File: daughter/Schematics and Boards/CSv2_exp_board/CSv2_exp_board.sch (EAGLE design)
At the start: 144 parts, among them J1 HIROSE-DF40_44-PIN_CONNECTORS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, J2 J-SERIAL-PORT, J3 CORTEX_DEBUG_SMD, J4 SJ-43514-SMT, J5 HIROSE-DF40_44-PIN_CONNECTORS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, J6 ATTINY_AVR_DEBUG, J7 J-USB-HIROSE-MICRO-USB, SW1 SPST_TACT-KMR2, SW2 SPST_TACT-KMR2, T1 TPTP10SQ, T10 TPTP10SQ, T11 TPTP10SQ, T2 TPTP10SQ, T3 TPTP10SQ, T4 TPTP10SQ, T5 TPTP10SQ, T6 TPTP10SQ, T7 TPTP10SQ, T8 TPTP10SQ, T9 TPTP10SQ, U1 LOADSWITCH-MIC94164, U10 LOADSWITCH-MIC94164, U11 BMI160, U12 TLV320DAC26IRHB, U13 ADG839YKSZ-500RL7KS_6_ADI-L, U14 LOADSWITCH-MIC94164, U15 LP2980AIM5-2.5/NOPBMF05A_TEX-L, U16 NCP553SQ18T1GSC-82AB_ONS-L, U17 ATTINY817-MFRQFN24_RX4MC-L_AT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, U18 MPL3115A2, U19 ATSAMD21G18_QFN, U2 ADA4841-1YRJZ-R7RJ_6-L, U3 Value, U4 RFM69HCW, U5 Value, U6 Value, U7 LOADSWITCH-MIC94164, U8 LOADSWITCH-MIC94164, U9 LOADSWITCH-MIC94164, X1 32.768kHz, X2 32.768, X3 uFL, X4 uFL, X5 uFL, X6 uFL

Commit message: DTR-filled in device attributes
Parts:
- X2: value 32.768 -> 32.768kHz; DESC (none) -> CRYSTAL 32.7680KHZ 6PF SMD; HEIGHT (none) -> 0.9mm; LOAD_CAPACITY 6p -> 6pF; SIZE (none) -> 0.126" L x 0.059" W (3.20mm x 1.50mm); TOL (none) -> ±20ppm; TYPE (none) -> Crystal
- X3, X5, X6: DESC (none) -> CONN U.FL RCPT STR 50 OHM SMD; HEIGHT d -> 1.25mm; MANUFACTURER (none) -> Hirose; SIZE (none) -> 3.1 x 3mm; TYPE (none) -> Connector
- X4: DESC (none) -> CONN U.FL RCPT STR 50 OHM SMD; HEIGHT (none) -> 1.25mm; MEANUFACTURER (none) -> Hirose; SIZE (none) -> 3.1 x 3mm; TYPE (none) -> Connector
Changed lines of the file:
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@@
 <attribute name="Z-HEIGHT" value="0.55mm"/>
 </part>
-<part name="X2" library="CommonSense-DTR-v1" deviceset="ADAFRUIT2_XTAL" device="-3.2X1.5" value="32.768">
-<attribute name="DESC" value=""/>
-<attribute name="LOAD_CAPACITY" value="6p"/>
+<part name="X2" library="CommonSense-DTR-v1" deviceset="ADAFRUIT2_XTAL" device="-3.2X1.5" value="32.768kHz">
+<attribute name="DESC" value="CRYSTAL 32.7680KHZ 6PF SMD"/>
+<attribute name="HEIGHT" value="0.9mm"/>
+<attribute name="LOAD_CAPACITY" value="6pF"/>
 <attribute name="MANUFACTURER" value="NDK"/>
 <attribute name="MPN" value="NX3215SA-32.768K-STD-MUA-14"/>
 <attribute name="PARTNO" value="NX3215SA-32.768K-STD-MUA-14"/>
-<attribute name="SIZE" value=""/>
-<attribute name="TOL" value=""/>
-<attribute name="TYPE" value=""/>
-<attribute name="VOLT" value=""/>
+<attribute name="SIZE" value="0.126&quot; L x 0.059&quot; W (3.20mm x 1.50mm)"/>
+<attribute name="TOL" value="±20ppm"/>
+<attribute name="TYPE" value="Crystal"/>
 </part>
 <part name="U$14" library="Supplies" deviceset="GND" device=""/>
@@
 <part name="U$17" library="Supplies" deviceset="GND" device=""/>
 <part name="X4" library="Connectors" deviceset="J-U.FL" device="" value="uFL">
-<attribute name="DESC" value=""/>
+<attribute name="DESC" value="CONN U.FL RCPT STR 50 OHM SMD"/>
+<attribute name="HEIGHT" value="1.25mm"/>
+<attribute name="MEANUFACTURER" value="Hirose"/>
 <attribute name="MPN" value="U.FL-R-SMT-1(01)"/>
 <attribute name="PARTNO" value="U.FL-R-SMT-1(01)"/>
-<attribute name="SIZE" value=""/>
-<attribute name="TOL" value=""/>
-<attribute name="TYPE" value=""/>
-<attribute name="VOLT" value=""/>
+<attribute name="SIZE" value="3.1 x 3mm"/>
+<attribute name="TYPE" value="Connector"/>
 </part>
 <part name="U$23" library="Supplies" deviceset="GND" device=""/>
@@
 </part>
 <part name="X3" library="Connectors" deviceset="J-U.FL" device="" value="uFL">
-<attribute name="HEIGHT" value="d"/>
+<attribute name="DESC" value="CONN U.FL RCPT STR 50 OHM SMD"/>
+<attribute name="HEIGHT" value="1.25mm"/>
+<attribute name="MANUFACTURER" value="Hirose"/>
 <attribute name="MPN" value="U.FL-R-SMT-1(01)"/>
 <attribute name="PARTNO" value="U.FL-R-SMT-1(01)"/>
+<attribute name="SIZE" value="3.1 x 3mm"/>
+<attribute name="TYPE" value="Connector"/>
 </part>
 <part name="X5" library="Connectors" deviceset="J-U.FL" device="" value="uFL">
-<attribute name="HEIGHT" value="d"/>
+<attribute name="DESC" value="CONN U.FL RCPT STR 50 OHM SMD"/>
+<attribute name="HEIGHT" value="1.25mm"/>
+<attribute name="MANUFACTURER" value="Hirose"/>
 <attribute name="MPN" value="U.FL-R-SMT-1(01)"/>
 <attribute name="PARTNO" value="U.FL-R-SMT-1(01)"/>
+<attribute name="SIZE" value="3.1 x 3mm"/>
+<attribute name="TYPE" value="Connector"/>
 </part>
 <part name="X6" library="Connectors" deviceset="J-U.FL" device="" value="uFL">
-<attribute name="HEIGHT" value="d"/>
+<attribute name="DESC" value="CONN U.FL RCPT STR 50 OHM SMD"/>
+<attribute name="HEIGHT" value="1.25mm"/>
+<attribute name="MANUFACTURER" value="Hirose"/>
 <attribute name="MPN" value="U.FL-R-SMT-1(01)"/>
 <attribute name="PARTNO" value="U.FL-R-SMT-1(01)"/>
+<attribute name="SIZE" value="3.1 x 3mm"/>
+<attribute name="TYPE" value="Connector"/>
 </part>
 <part name="R7" library="Resistors" deviceset="R-" device="0402" value="50R">
@@
 <attribute name="TYPE" x="284.48" y="231.14" size="1.778" layer="96" display="off"/>
 <attribute name="SIZE" x="284.48" y="231.14" size="1.778" layer="96" display="off"/>
-<attribute name="VOLT" x="284.48" y="231.14" size="1.778" layer="96" display="off"/>
+<attribute name="HEIGHT" x="284.48" y="231.14" size="1.778" layer="96" display="off"/>
 </instance>
 <instance part="U$14" gate="1" x="101.6" y="233.68" smashed="yes">
@@
 <attribute name="MPN" x="78.62295625" y="212.957171875" size="1.778" layer="96" rot="R90" display="off"/>
 <attribute name="PARTNO" x="78.62295625" y="212.957171875" size="1.778" layer="96" display="off"/>
-<attribute name="TOL" x="78.62295625" y="212.957171875" size="1.778" layer="96" rot="R90" display="off"/>
 <attribute name="DESC" x="78.62295625" y="212.957171875" size="1.778" layer="96" rot="R90" display="off"/>
 <attribute name="TYPE" x="78.62295625" y="212.957171875" size="1.778" layer="96" rot="R90" display="off"/>
 <attribute name="SIZE" x="78.62295625" y="212.957171875" size="1.778" layer="96" rot="R90" display="off"/>
-<attribute name="VOLT" x="78.62295625" y="212.957171875" size="1.778" layer="96" rot="R90" display="off"/>
+<attribute name="HEIGHT" x="78.62295625" y="212.957171875" size="1.778" layer="96" rot="R90" display="off"/>
+<attribute name="MEANUFACTURER" x="78.62295625" y="212.957171875" size="1.778" layer="96" rot="R90" display="off"/>
 </instance>
 <instance part="U$23" gate="1" x="68.58" y="215.9" smashed="yes">
@@
 <attribute name="MPN" x="266.58295625" y="248.517171875" size="1.778" layer="96" rot="R90" display="off"/>
 <attribute name="PARTNO" x="266.58295625" y="248.517171875" size="1.778" layer="96" display="off"/>
+<attribute name="SIZE" x="266.58295625" y="248.517171875" size="1.778" layer="96" rot="R90" display="off"/>
+<attribute name="DESC" x="266.58295625" y="248.517171875" size="1.778" layer="96" rot="R90" display="off"/>
+<attribute name="TYPE" x="266.58295625" y="248.517171875" size="1.778" layer="96" rot="R90" display="off"/>
+<attribute name="MANUFACTURER" x="266.58295625" y="248.517171875" size="1.778" layer="96" rot="R90" display="off"/>
 <attribute name="HEIGHT" x="266.58295625" y="248.517171875" size="1.778" layer="96" rot="R90" display="off"/>
 </instance>
@@
 <attribute name="MPN" x="297.06295625" y="248.517171875" size="1.778" layer="96" rot="R90" display="off"/>
 <attribute name="PARTNO" x="297.06295625" y="248.517171875" size="1.778" layer="96" display="off"/>
+<attribute name="SIZE" x="297.06295625" y="248.517171875" size="1.778" layer="96" rot="R90" display="off"/>
+<attribute name="DESC" x="297.06295625" y="248.517171875" size="1.778" layer="96" rot="R90" display="off"/>
+<attribute name="TYPE" x="297.06295625" y="248.517171875" size="1.778" layer="96" rot="R90" display="off"/>
+<attribute name="MANUFACTURER" x="297.06295625" y="248.517171875" size="1.778" layer="96" rot="R90" display="off"/>
 <attribute name="HEIGHT" x="297.06295625" y="248.517171875" size="1.778" layer="96" rot="R90" display="off"/>
 </instance>
@@
 <attribute name="MPN" x="330.08295625" y="248.517171875" size="1.778" layer="96" rot="R90" display="off"/>
 <attribute name="PARTNO" x="330.08295625" y="248.517171875" size="1.778" layer="96" display="off"/>
+<attribute name="SIZE" x="330.08295625" y="248.517171875" size="1.778" layer="96" rot="R90" display="off"/>
+<attribute name="DESC" x="330.08295625" y="248.517171875" size="1.778" layer="96" rot="R90" display="off"/>
+<attribute name="TYPE" x="330.08295625" y="248.517171875" size="1.778" layer="96" rot="R90" display="off"/>
+<attribute name="MANUFACTURER" x="330.08295625" y="248.517171875" size="1.778" layer="96" rot="R90" display="off"/>
 <attribute name="HEIGHT" x="330.08295625" y="248.517171875" size="1.778" layer="96" rot="R90" display="off"/>
 </instance>

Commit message: DTR-v1.1 after moving LoRa to the top
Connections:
- net +3V3_RFM_PWR: now also U6.COM2; no longer U6.COM1
- net +3V3_SAMD_PWR: now also U6.COM1; no longer U6.COM2
- net MEAS_RFM: now also U6.IN2; no longer U6.IN1
- net MEAS_SAMD: now also U6.IN1; no longer U6.IN2
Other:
- moved on the sheet: C10, C11, C17, C18, JP1, JP10, JP11, JP2, U1, U7

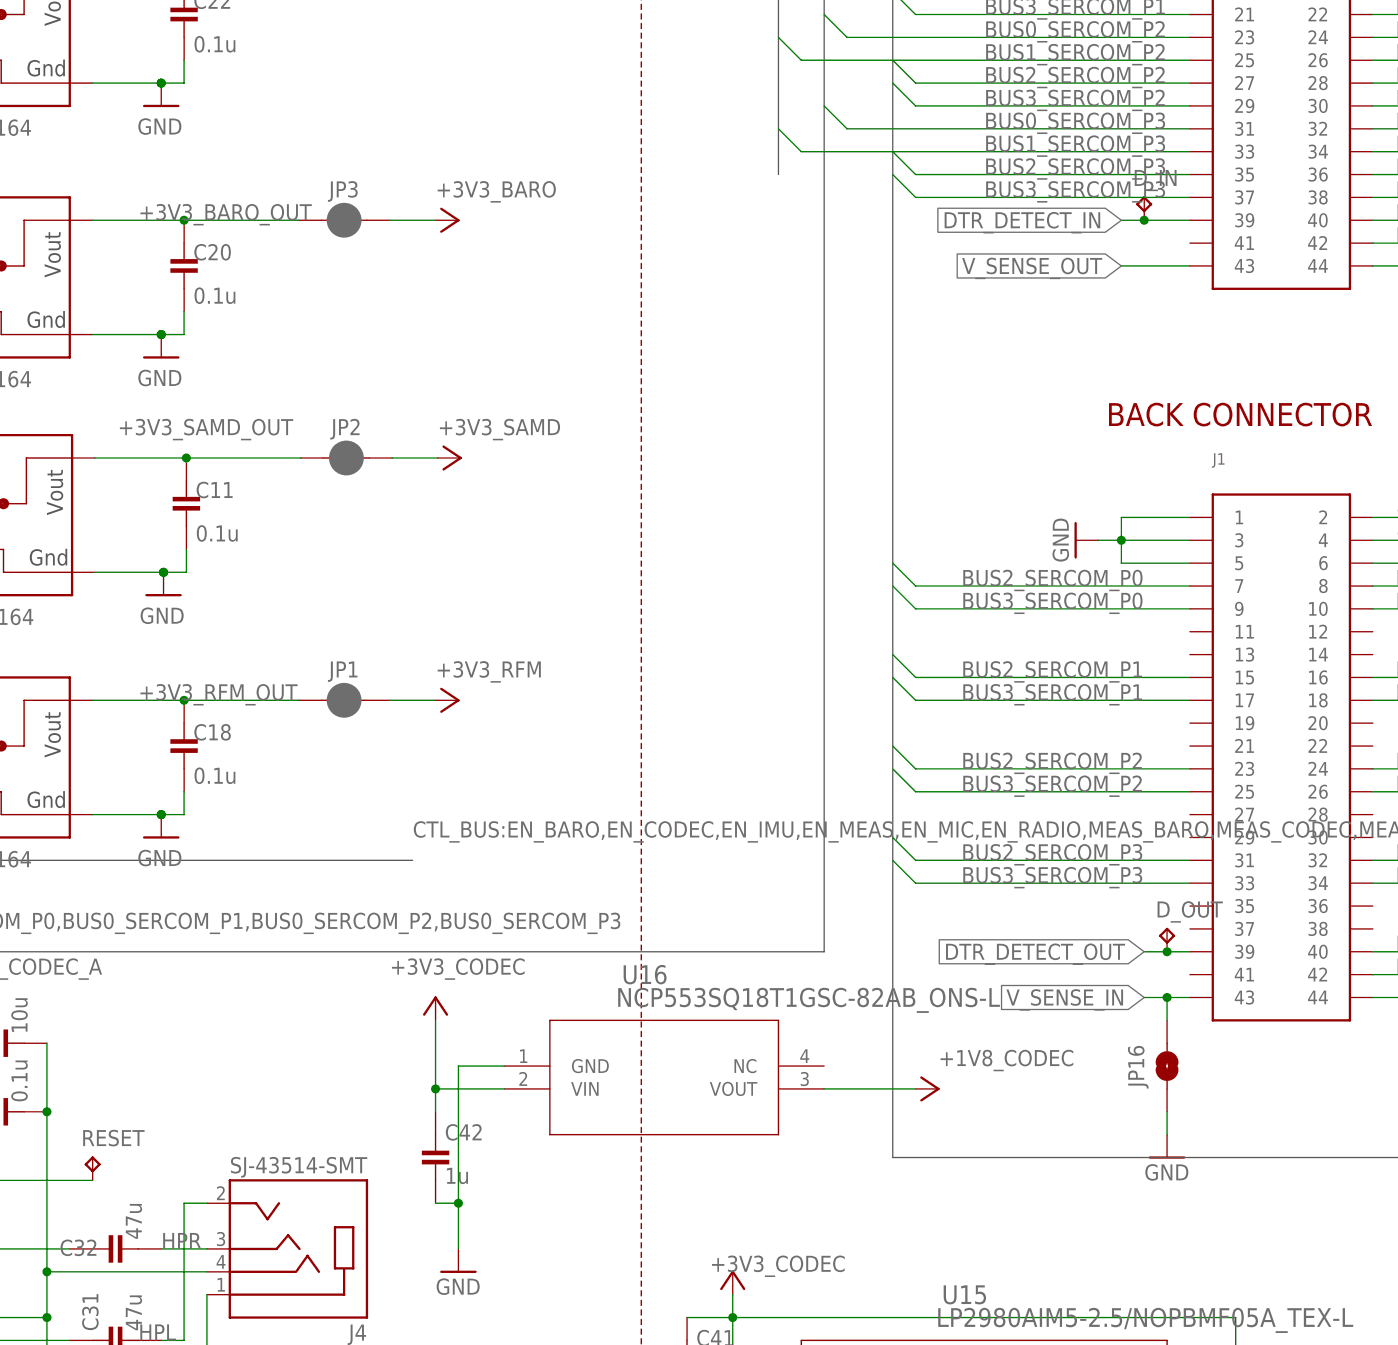
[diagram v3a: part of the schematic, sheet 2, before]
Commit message: DTR-rounded inner corners, adjusted silkscreen texts, added CAM/gerber
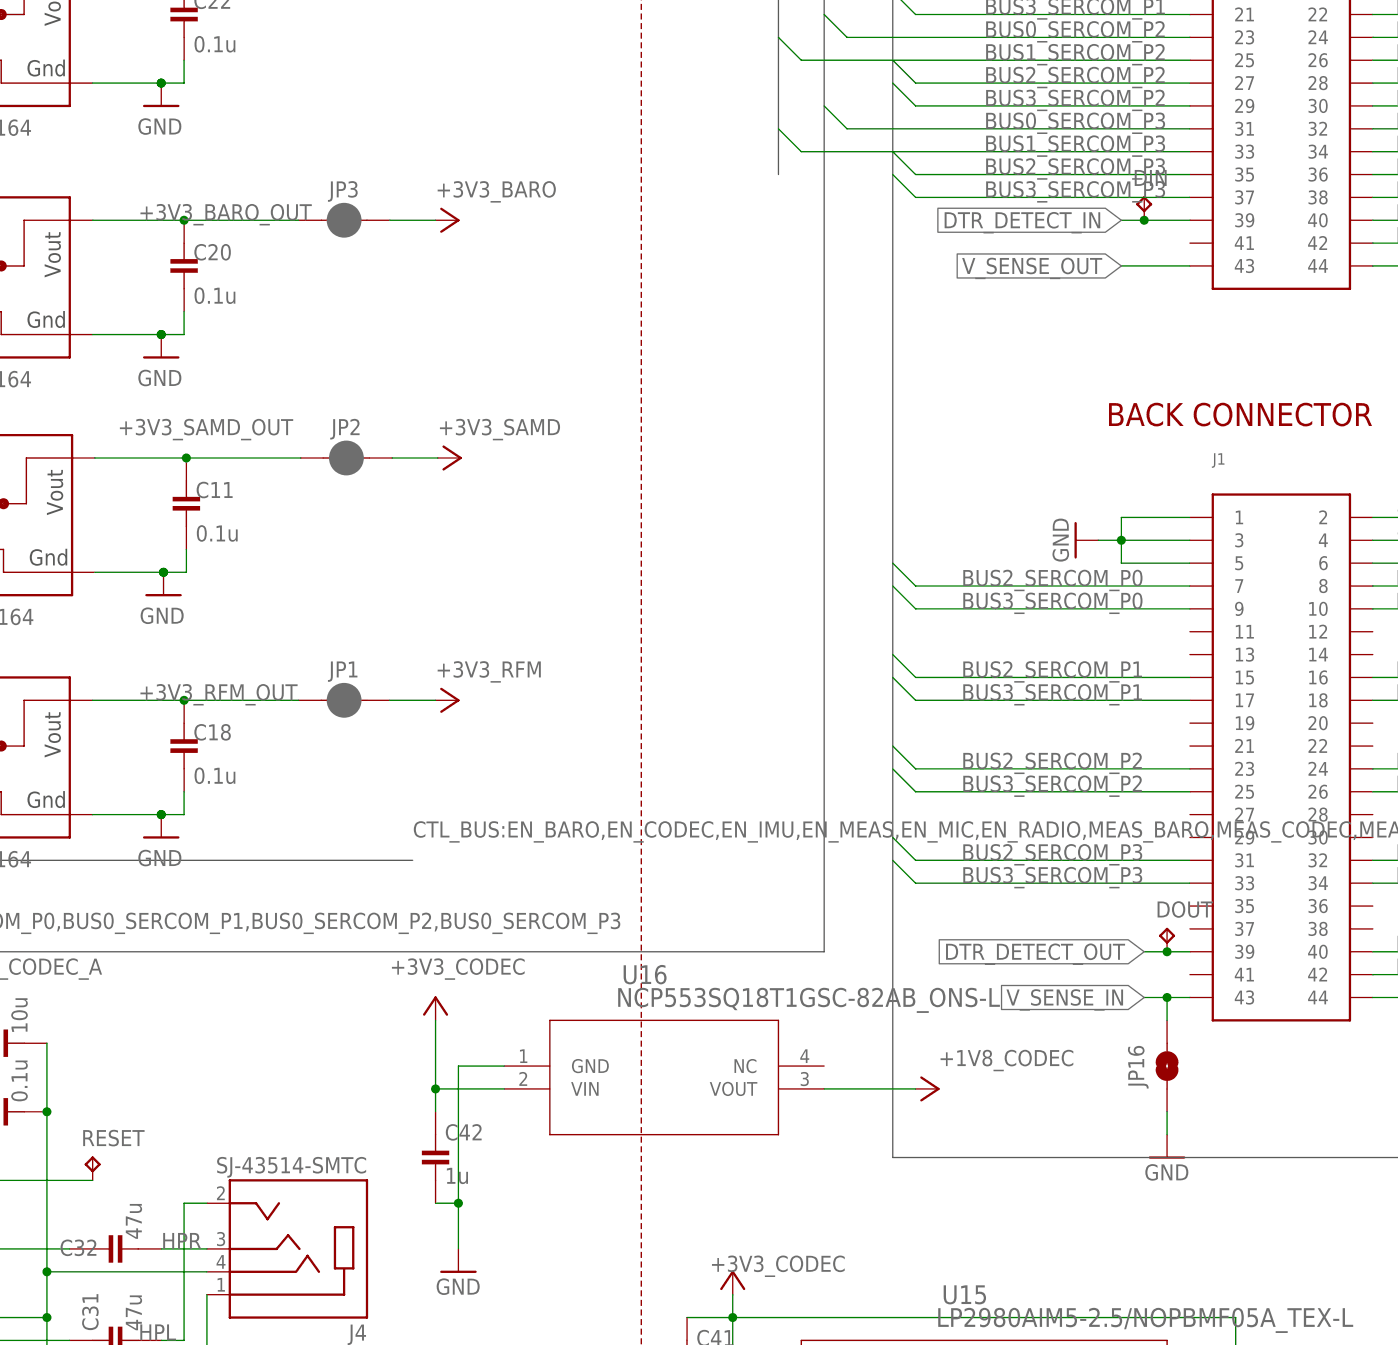
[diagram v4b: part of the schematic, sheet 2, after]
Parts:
- J4: value SJ-43514-SMT -> SJ-43514-SMTC; device CommonSense-DTR-v1:SJ-43514-SMT -> CommonSense-DTR-v1:SJ-43514-SMTC
- U4: device Radios:RFM95C -> CommonSense-DTR-v1:RFM95C
- renumbered D_IN to DIN, D_OUT to DOUT
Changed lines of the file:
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@@
 </part>
 <part name="+3V5" library="Supplies" deviceset="+3V3" device=""/>
-<part name="U4" library="Radios" deviceset="RFM95" device="C" value="RFM69HCW">
+<part name="U4" library="CommonSense-DTR-v1" deviceset="RFM95" device="C" value="RFM69HCW">
 <attribute name="DESC" value="RX TXRX MODULE ISM &lt; 1GHZ SMD"/>
 <attribute name="MPN" value="RFM95CW"/>
@@
 </part>
 <part name="GND25" library="Supplies" deviceset="GND" device=""/>
-<part name="D_IN" library="TestPoints" deviceset="TP" device="TP10SQ" package3d_urn="urn:adsk.eagle:package:27962/1" value="TPTP10SQ">
+<part name="DIN" library="TestPoints" deviceset="TP" device="TP10SQ" package3d_urn="urn:adsk.eagle:package:27962/1" value="TPTP10SQ">
 <attribute name="PARTNO" value="*"/>
 <attribute name="Z-HEIGHT" value="d"/>
@@
 <attribute name="Z-HEIGHT" value="d"/>
 </part>
-<part name="D_OUT" library="TestPoints" deviceset="TP" device="TP10SQ" package3d_urn="urn:adsk.eagle:package:27962/1" value="TPTP10SQ">
+<part name="DOUT" library="TestPoints" deviceset="TP" device="TP10SQ" package3d_urn="urn:adsk.eagle:package:27962/1" value="TPTP10SQ">
 <attribute name="PARTNO" value="*"/>
 <attribute name="Z-HEIGHT" value="d"/>
@@
 <attribute name="TYPE" value="Codec"/>
 </part>
-<part name="J4" library="CommonSense-DTR-v1" deviceset="SJ-43514-SMT" device="">
+<part name="J4" library="CommonSense-DTR-v1" deviceset="SJ-43514-SMT" device="C" value="SJ-43514-SMTC">
 <attribute name="DESC" value="CONN JACK 4COND 3.5MM SMD R/A"/>
 <attribute name="HEIGHT" value="5mm"/>
@@
 <attribute name="VALUE" x="292.1" y="48.26" size="1.778" layer="96"/>
 </instance>
-<instance part="D_IN" gate="G$1" x="292.1" y="157.48" smashed="yes">
+<instance part="DIN" gate="G$1" x="292.1" y="157.48" smashed="yes">
 <attribute name="NAME" x="290.83" y="158.75" size="1.778" layer="95"/>
 <attribute name="TP_SIGNAL_NAME" x="293.37" y="156.21" size="1.778" layer="97"/>
@@
 <attribute name="Z-HEIGHT" x="322.58" y="152.4" size="1.778" layer="96" display="off"/>
 </instance>
-<instance part="D_OUT" gate="G$1" x="294.64" y="76.2" smashed="yes">
+<instance part="DOUT" gate="G$1" x="294.64" y="76.2" smashed="yes">
 <attribute name="NAME" x="293.37" y="77.47" size="1.778" layer="95"/>
 <attribute name="TP_SIGNAL_NAME" x="295.91" y="74.93" size="1.778" layer="97"/>
@@
 <wire x1="297.18" y1="154.94" x2="292.1" y2="154.94" width="0.1524" layer="91"/>
 <label x="289.56" y="154.94" size="1.778" layer="95" rot="R180" xref="yes"/>
-<pinref part="D_IN" gate="G$1" pin="TP"/>
+<pinref part="DIN" gate="G$1" pin="TP"/>
 <wire x1="292.1" y1="154.94" x2="289.56" y2="154.94" width="0.1524" layer="91"/>
 <junction x="292.1" y="154.94"/>
@@
 <wire x1="297.18" y1="73.66" x2="294.64" y2="73.66" width="0.1524" layer="91"/>
 <label x="292.1" y="73.66" size="1.778" layer="95" rot="R180" xref="yes"/>
-<pinref part="D_OUT" gate="G$1" pin="TP"/>
+<pinref part="DOUT" gate="G$1" pin="TP"/>
 <wire x1="294.64" y1="73.66" x2="292.1" y2="73.66" width="0.1524" layer="91"/>
 <junction x="294.64" y="73.66"/>
